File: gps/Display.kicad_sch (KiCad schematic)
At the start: 8 parts, among them U4 HT16k33, U5 7seg_1x1_rgb, U6 7seg_1x1_rgb, U7 7seg_1x1_rgb, U8 KW4-804AGB

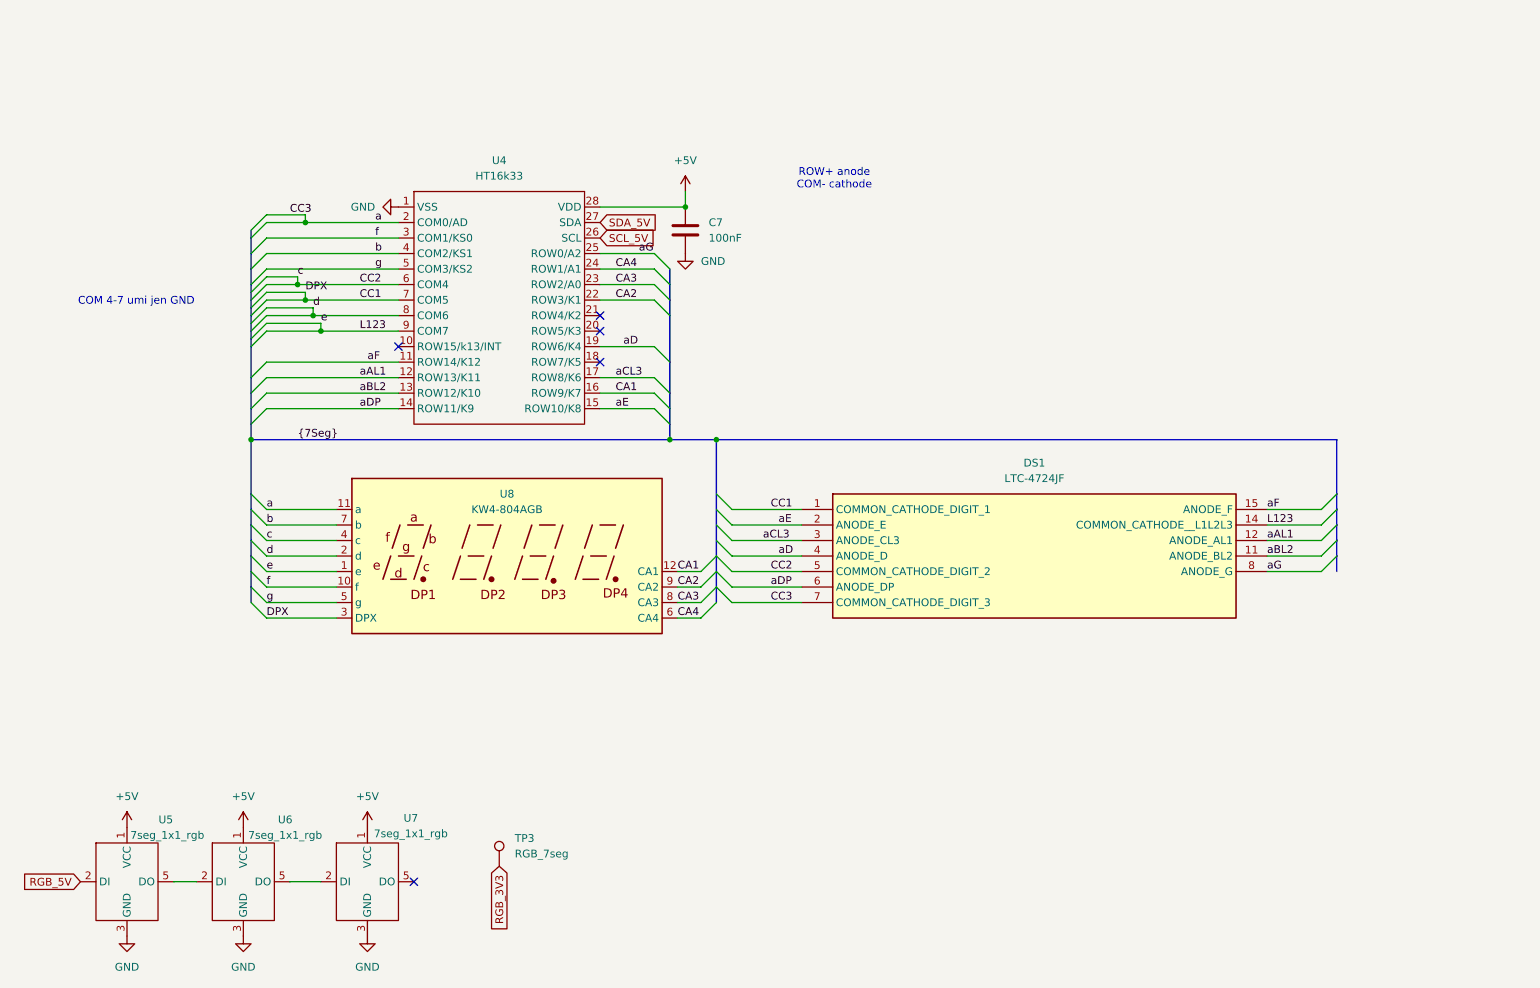
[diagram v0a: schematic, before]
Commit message: Final V1, cleaned display connections
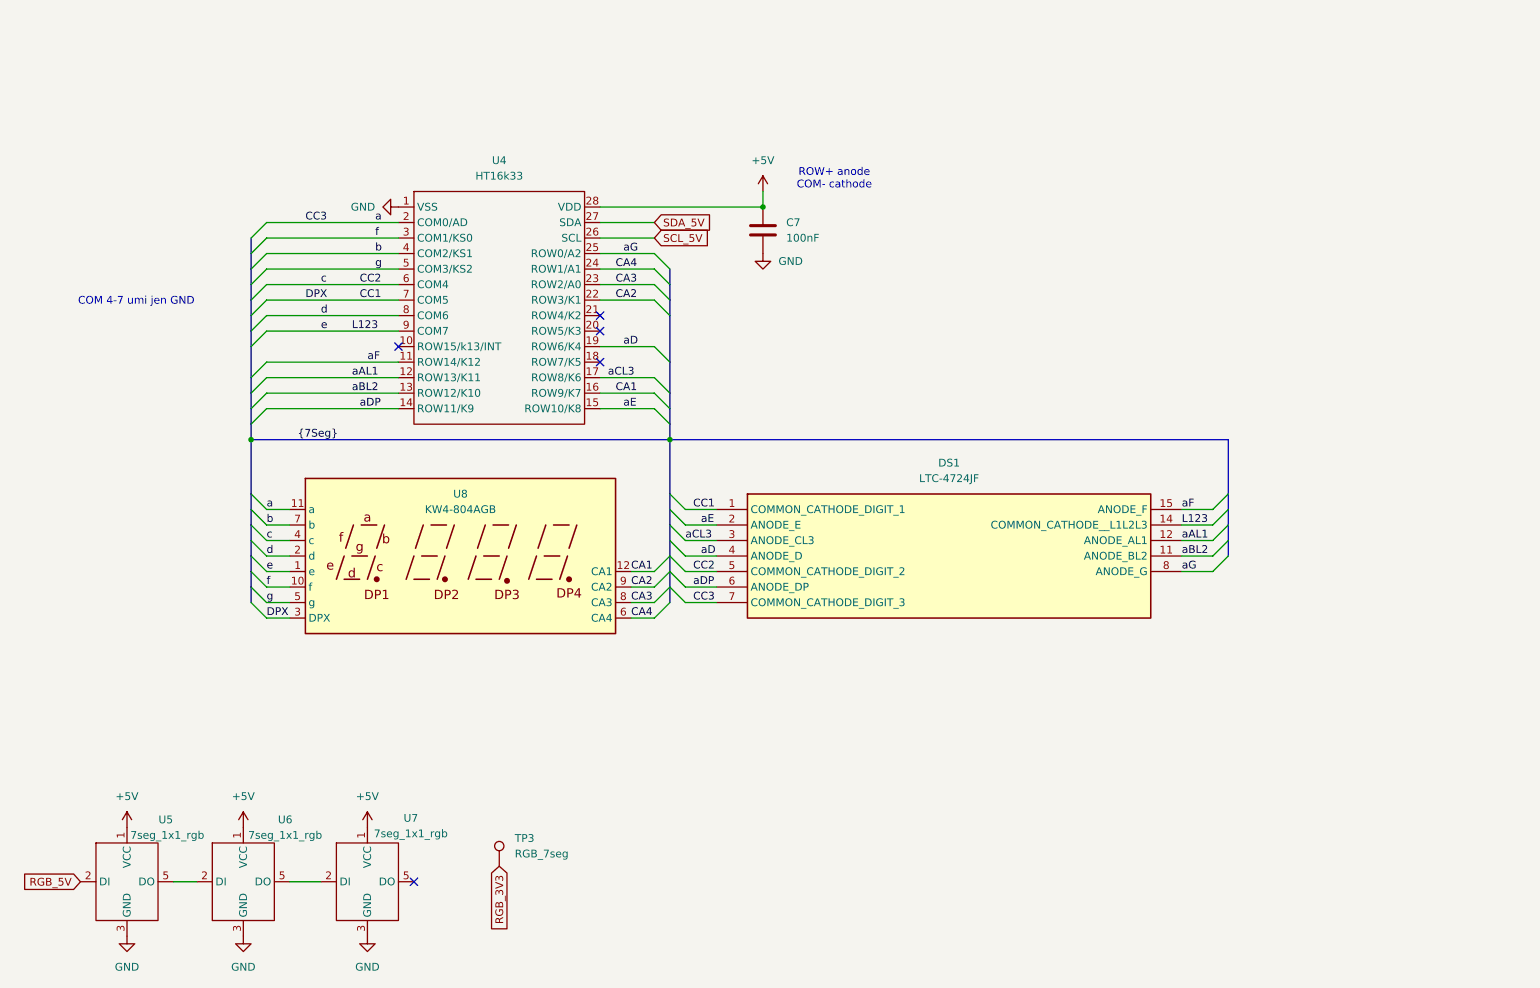
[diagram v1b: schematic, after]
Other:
- moved on the sheet: C7, DS1, U8

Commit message: cleaned schematic
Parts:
- added C4, C5, C6: 10uF, Capacitor_SMD:C_0603_1608Metric_Pad1.08x0.95mm_HandSolder, symbol Device:C
- added D2: B120-E3, Diode_SMD:D_SMA, symbol Diode:B120-E3
- added L2: 2.2 uH, Inductor_SMD:L_1008_2520Metric_Pad1.43x2.20mm_HandSolder, symbol Device:L
- added R1: 0R, Resistor_SMD:R_0805_2012Metric_Pad1.20x1.40mm_HandSolder, symbol Device:R
- added TP6: +5V, TestPoint:TestPoint_Loop_D1.80mm_Drill1.0mm_Beaded, symbol Connector:TestPoint
- added U2: TPS613222ADBVR, Package_TO_SOT_SMD:SOT-23-5, symbol Regulator_Switching:TPS613226ADBV
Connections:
- net +5V: now also R1.2
- net GND: now also C4.2, C5.2, C6.2, U2.2 (GND)
- new net: C5.1, C6.1, D2.1 (K), R1.1, TP6.1, U2.4 (VOUT)
- new net: D2.2 (A), L2.2, U2.1 (SW)
- new net VCC: C4.1, L2.1
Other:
- note added: "7seg displays and 7seg driver"
- note added: "DC/DC"
- note added: "RGB 7seg displays"
- note removed: "COM 4-7 umi jen GND"
- moved on the sheet: C7, TP3, U4, U5, U6, U7, U8

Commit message: updated pdf/
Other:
- title: (none) -> GNSS_Geret
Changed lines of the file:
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@@
 	(generator_version "8.0")
 	(paper "A4")
+	(title_block
+		(title "GNSS_Geret")
+		(rev "1")
+	)
 	(bus_alias "7Seg"
 		(members "a" "b" "c" "d" "e" "f" "g" "DPX" "CA1" "CA2" "CA3" "CA4" "CC1"
